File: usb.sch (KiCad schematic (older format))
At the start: 15 parts, among them J3 USB_OTG, Q1 BC817, U2 STMPS2151STR

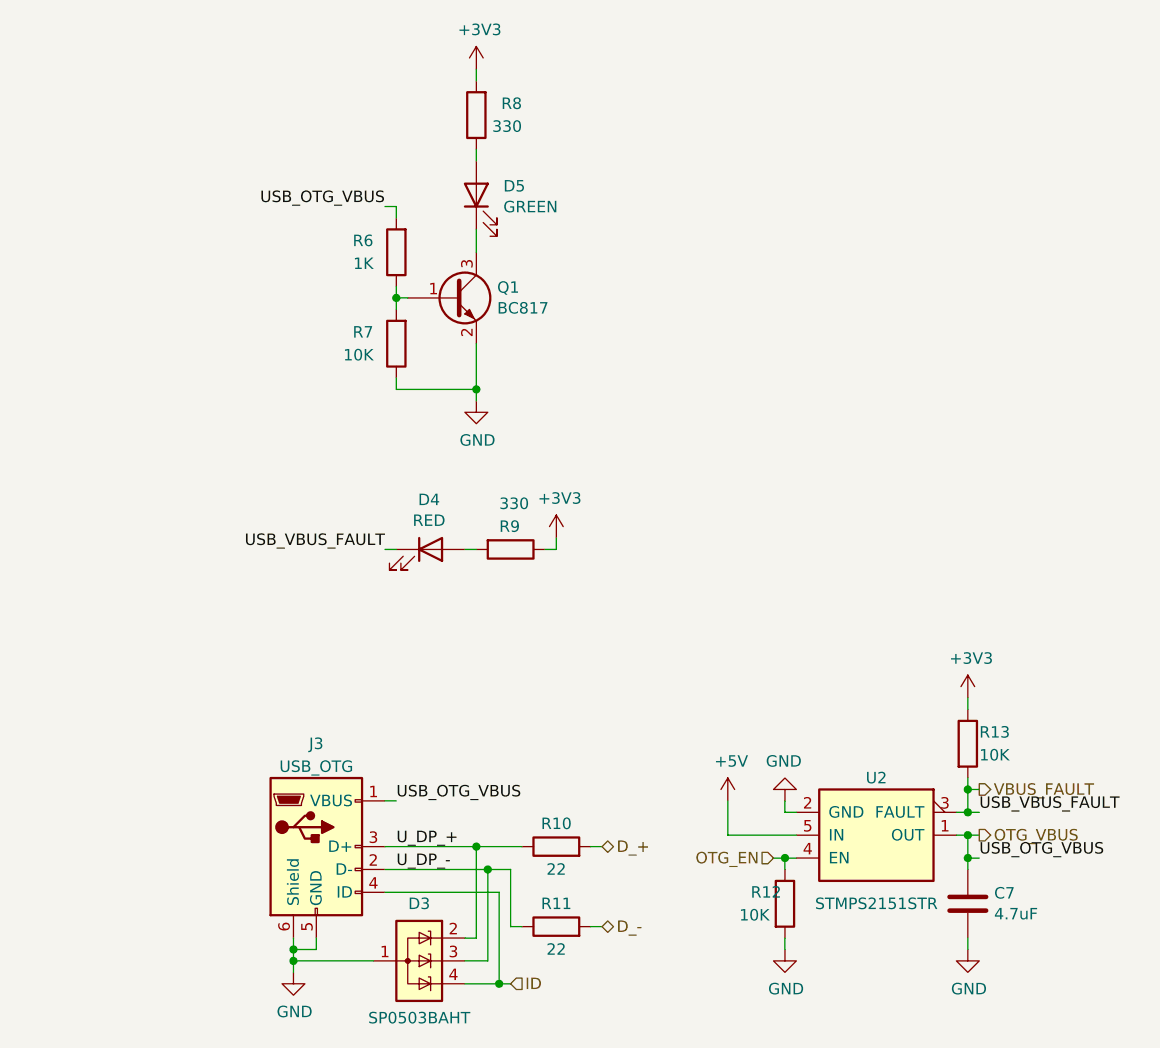
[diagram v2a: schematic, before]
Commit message: dcdc доделан на 5V.
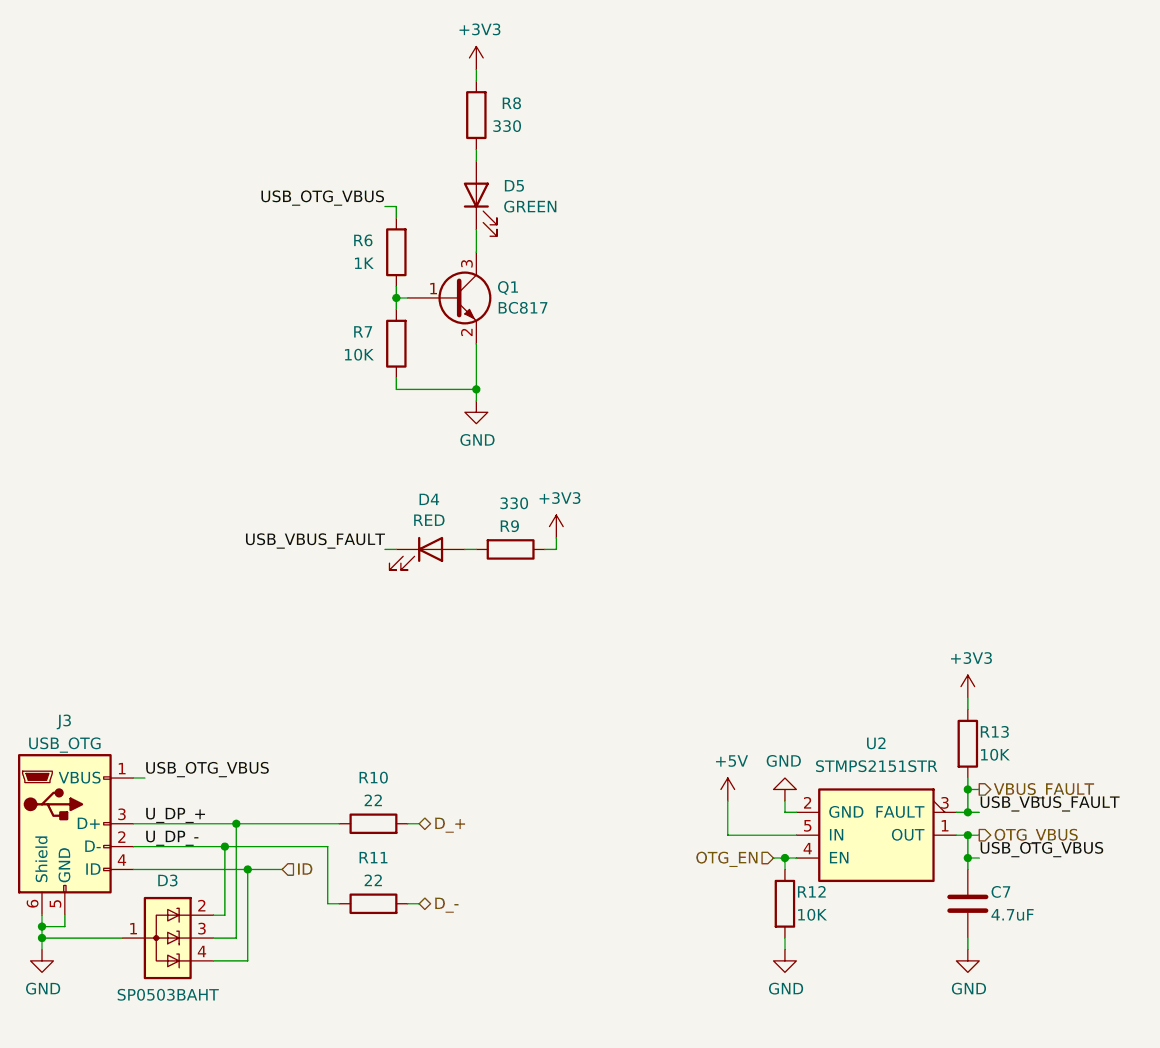
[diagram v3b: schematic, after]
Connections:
- net U_DP_+: now also D3.3 (K); no longer D3.2 (K)
- net U_DP_-: now also D3.2 (K); no longer D3.3 (K)
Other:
- moved on the sheet: D3, J3, R10, R11
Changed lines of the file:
@@
 U 1 1 5EBF34AD
 P 6900 4550
-F 0 "U2" H 7150 4600 50  0000 C CNN
-F 1 "STMPS2151STR" H 7150 4050 50  0000 C CNN
+F 0 "U2" H 7150 4750 50  0000 C CNN
+F 1 "STMPS2151STR" H 7150 4650 50  0000 C CNN
 F 2 "Package_TO_SOT_SMD:SOT-23-5_HandSoldering" H 6950 4600 50  0001 C CNN
 F 3 "" H 6950 4600 50  0001 C CNN
@@
 U 1 1 5EBF34C5
 P 6750 5050
-F 0 "R12" H 6600 5100 50  0000 L CNN
-F 1 "10K" H 6550 5000 50  0000 L CNN
+F 0 "R12" H 6800 5100 50  0000 L CNN
+F 1 "10K" H 6800 5000 50  0000 L CNN
 F 2 "Resistor_SMD:R_0603_1608Metric_Pad1.05x0.95mm_HandSolder" V 6680 5050 50  0001 C CNN
 F 3 "~" H 6750 5050 50  0001 C CNN
@@
 U 1 1 5EBF34D7
 P 7550 5050
-F 0 "C7" H 7665 5096 50  0000 L CNN
-F 1 "4.7uF" H 7665 5005 50  0000 L CNN
+F 0 "C7" H 7650 5100 50  0000 L CNN
+F 1 "4.7uF" H 7650 5000 50  0000 L CNN
 F 2 "Capacitor_SMD:C_0603_1608Metric_Pad1.05x0.95mm_HandSolder" H 7588 4900 50  0001 C CNN
 F 3 "~" H 7550 5050 50  0001 C CNN
@@
 L Connector:USB_OTG J3
 U 1 1 5EBF354C
-P 4700 4800
-F 0 "J3" H 4700 5250 50  0000 C CNN
-F 1 "USB_OTG" H 4700 5150 50  0000 C CNN
-F 2 "Connector_USB:USB_Mini-B_Wuerth_65100516121_Horizontal" H 4850 4750 50  0001 C CNN
-F 3 " ~" H 4850 4750 50  0001 C CNN
-	1    4700 4800
-	1    0    0    -1
-$EndComp
-Wire Wire Line
-	5000 4800 5400 4800
-Wire Wire Line
-	5400 5200 5400 4800
-Connection ~ 5400 4800
-Wire Wire Line
-	5400 4800 5600 4800
-Connection ~ 4600 5300
-Wire Wire Line
-	4600 5350 4600 5300
-Wire Wire Line
-	4600 5300 4950 5300
-Wire Wire Line
-	5450 4900 5550 4900
-Connection ~ 5450 4900
-Wire Wire Line
-	5450 5300 5450 4900
-Connection ~ 5500 5400
-Wire Wire Line
-	5350 5400 5500 5400
-Wire Wire Line
-	5000 5000 5500 5000
-Wire Wire Line
-	5500 5400 5550 5400
-Wire Wire Line
-	5500 5000 5500 5400
-Wire Wire Line
-	5900 5150 5950 5150
-Wire Wire Line
-	5900 4800 5950 4800
-Wire Wire Line
-	5550 5150 5600 5150
-Wire Wire Line
-	5550 4900 5550 5150
-Wire Wire Line
-	5000 4900 5450 4900
+P 3600 4700
+F 0 "J3" H 3600 5150 50  0000 C CNN
+F 1 "USB_OTG" H 3600 5050 50  0000 C CNN
+F 2 "Connector_USB:USB_Mini-B_Wuerth_65100516121_Horizontal" H 3750 4650 50  0001 C CNN
+F 3 " ~" H 3750 4650 50  0001 C CNN
+	1    3600 4700
+	1    0    0    -1
+$EndComp
+Connection ~ 3500 5200
+Wire Wire Line
+	3500 5250 3500 5200
+Wire Wire Line
+	3500 5200 3850 5200
+Wire Wire Line
+	5100 5050 5150 5050
+Wire Wire Line
+	5100 4700 5150 4700
+Wire Wire Line
+	4750 5050 4800 5050
+Wire Wire Line
+	4750 4800 4750 5050
 $Comp
 L Device:R R10
 U 1 1 5EBF356B
-P 5750 4800
-F 0 "R10" V 5850 4800 50  0000 C CNN
-F 1 "22" V 5650 4800 50  0000 C CNN
-F 2 "Resistor_SMD:R_0603_1608Metric_Pad1.05x0.95mm_HandSolder" V 5680 4800 50  0001 C CNN
-F 3 "~" H 5750 4800 50  0001 C CNN
-	1    5750 4800
+P 4950 4700
+F 0 "R10" V 5150 4700 50  0000 C CNN
+F 1 "22" V 5050 4700 50  0000 C CNN
+F 2 "Resistor_SMD:R_0603_1608Metric_Pad1.05x0.95mm_HandSolder" V 4880 4700 50  0001 C CNN
+F 3 "~" H 4950 4700 50  0001 C CNN
+	1    4950 4700
 	0    -1   -1   0
 $EndComp
-Connection ~ 4600 5250
-Wire Wire Line
-	4600 5300 4600 5250
+Connection ~ 3500 5150
+Wire Wire Line
+	3500 5200 3500 5150
 $Comp
 L power:GND #PWR012
 U 1 1 5EBF3573
-P 4600 5350
-F 0 "#PWR012" H 4600 5100 50  0001 C CNN
-F 1 "GND" H 4605 5177 50  0000 C CNN
-F 2 "" H 4600 5350 50  0001 C CNN
-F 3 "" H 4600 5350 50  0001 C CNN
-	1    4600 5350
-	1    0    0    -1
-$EndComp
-Wire Wire Line
-	4700 5250 4700 5200
-Wire Wire Line
-	4600 5250 4700 5250
-Wire Wire Line
-	4600 5200 4600 5250
+P 3500 5250
+F 0 "#PWR012" H 3500 5000 50  0001 C CNN
+F 1 "GND" H 3505 5077 50  0000 C CNN
+F 2 "" H 3500 5250 50  0001 C CNN
+F 3 "" H 3500 5250 50  0001 C CNN
+	1    3500 5250
+	1    0    0    -1
+$EndComp
+Wire Wire Line
+	3600 5150 3600 5100
+Wire Wire Line
+	3500 5150 3600 5150
+Wire Wire Line
+	3500 5100 3500 5150
 $Comp
 L Power_Protection:SP0503BAHT D3
 U 1 1 5EBF357C
-P 5150 5300
-F 0 "D3" V 4900 5300 50  0000 C CNN
-F 1 "SP0503BAHT" V 5400 5300 50  0000 C CNN
-F 2 "Package_TO_SOT_SMD:SOT-143_Handsoldering" H 5375 5250 50  0001 L CNN
-F 3 "http://www.littelfuse.com/~/media/files/littelfuse/technical%20resources/documents/data%20sheets/sp05xxba.pdf" H 5275 5425 50  0001 C CNN
-	1    5150 5300
+P 4050 5200
+F 0 "D3" V 3800 5200 50  0000 C CNN
+F 1 "SP0503BAHT" V 4300 5200 50  0000 C CNN
+F 2 "Package_TO_SOT_SMD:SOT-143_Handsoldering" H 4275 5150 50  0001 L CNN
+F 3 "http://www.littelfuse.com/~/media/files/littelfuse/technical%20resources/documents/data%20sheets/sp05xxba.pdf" H 4175 5325 50  0001 C CNN
+	1    4050 5200
 	0    1    1    0
 $EndComp
@@
 L Device:R R11
 U 1 1 5EBF3583
-P 5750 5150
-F 0 "R11" V 5850 5150 50  0000 C CNN
-F 1 "22" V 5650 5150 50  0000 C CNN
-F 2 "Resistor_SMD:R_0603_1608Metric_Pad1.05x0.95mm_HandSolder" V 5680 5150 50  0001 C CNN
-F 3 "~" H 5750 5150 50  0001 C CNN
-	1    5750 5150
+P 4950 5050
+F 0 "R11" V 5150 5050 50  0000 C CNN
+F 1 "22" V 5050 5050 50  0000 C CNN
+F 2 "Resistor_SMD:R_0603_1608Metric_Pad1.05x0.95mm_HandSolder" V 4880 5050 50  0001 C CNN
+F 3 "~" H 4950 5050 50  0001 C CNN
+	1    4950 5050
 	0    -1   -1   0
 $EndComp
 Wire Wire Line
-	5000 4600 5050 4600
+	3900 4500 3950 4500
 Text HLabel 7600 4550 2    50   Output ~ 0
 VBUS_FAULT
@@
 Text Label 7600 4850 0    50   ~ 0
 USB_OTG_VBUS
-Text Label 5050 4600 0    50   ~ 0
+Text Label 3950 4500 0    50   ~ 0
 USB_OTG_VBUS
-Text HLabel 5950 4800 2    50   BiDi ~ 0
+Text HLabel 5150 4700 2    50   BiDi ~ 0
 D_+
-Text HLabel 5950 5150 2    50   BiDi ~ 0
+Text HLabel 5150 5050 2    50   BiDi ~ 0
 D_-
-Text HLabel 5550 5400 2    50   Input ~ 0
+Text HLabel 4550 4900 2    50   Input ~ 0
 ID
 Text Label 7600 4650 0    50   ~ 0
@@
 	5400 2800 5400 2850
 Connection ~ 5400 2800
-Text Label 5050 4800 0    50   ~ 0
+Text Label 3950 4700 0    50   ~ 0
 U_DP_+
-Text Label 5050 4900 0    50   ~ 0
+Text Label 3950 4800 0    50   ~ 0
 U_DP_-
 Wire Wire Line
-	5350 5300 5450 5300
-Wire Wire Line
-	5350 5200 5400 5200
+	4250 5100 4300 5100
+Wire Wire Line
+	4250 5300 4400 5300
+Wire Wire Line
+	4400 4900 4550 4900
+Wire Wire Line
+	3900 4900 4400 4900
+Connection ~ 4400 4900
+Wire Wire Line
+	3900 4700 4350 4700
+Wire Wire Line
+	3900 4800 4300 4800
+Wire Wire Line
+	4300 5100 4300 4800
+Connection ~ 4300 4800
+Wire Wire Line
+	4300 4800 4750 4800
+Wire Wire Line
+	4400 4900 4400 5300
+Wire Wire Line
+	4250 5200 4350 5200
+Wire Wire Line
+	4350 5200 4350 4700
+Connection ~ 4350 4700
+Wire Wire Line
+	4350 4700 4800 4700
 $EndSCHEMATC

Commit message: Расставил проверенные блоки в столбец.
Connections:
- net OTG_VBUS renamed VDD_USB
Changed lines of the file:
@@
 $Descr A4 11693 8268
 encoding utf-8
-Sheet 9 12
+Sheet 8 12
 Title ""
 Date ""
@@
 $EndComp
 Wire Wire Line
-	7550 4900 7550 4850
-Wire Wire Line
 	7550 4750 7600 4750
 Connection ~ 7550 4750
@@
 U 1 1 5EBF34F9
 P 5200 3500
-F 0 "D4" H 5193 3717 50  0000 C CNN
-F 1 "RED" H 5193 3626 50  0000 C CNN
+F 0 "D4" H 5200 3700 50  0000 C CNN
+F 1 "RED" H 5200 3600 50  0000 C CNN
 F 2 "LED_SMD:LED_0603_1608Metric_Pad1.05x0.95mm_HandSolder" H 5200 3500 50  0001 C CNN
 F 3 "~" H 5200 3500 50  0001 C CNN
@@
 U 1 1 5EBF34FF
 P 5550 3500
-F 0 "R9" V 5450 3450 50  0000 L CNN
-F 1 "330" V 5350 3450 50  0000 L CNN
+F 0 "R9" V 5350 3450 50  0000 L CNN
+F 1 "330" V 5450 3425 50  0000 L CNN
 F 2 "Resistor_SMD:R_0603_1608Metric_Pad1.05x0.95mm_HandSolder" V 5480 3500 50  0001 C CNN
 F 3 "~" H 5550 3500 50  0001 C CNN
@@
 P 5750 3450
 F 0 "#PWR015" H 5750 3300 50  0001 C CNN
-F 1 "+3V3" H 5765 3623 50  0000 C CNN
+F 1 "+3V3" H 5750 3650 50  0000 C CNN
 F 2 "" H 5750 3450 50  0001 C CNN
 F 3 "" H 5750 3450 50  0001 C CNN
@@
 U 1 1 5EBF3510
 P 5050 2200
-F 0 "R6" H 5150 2150 50  0000 L CNN
-F 1 "1K" H 5150 2250 50  0000 L CNN
+F 0 "R6" H 4900 2150 50  0000 L CNN
+F 1 "1K" H 4900 2250 50  0000 L CNN
 F 2 "Resistor_SMD:R_0603_1608Metric_Pad1.05x0.95mm_HandSolder" V 4980 2200 50  0001 C CNN
 F 3 "~" H 5050 2200 50  0001 C CNN
@@
 U 1 1 5EBF3516
 P 5050 2600
-F 0 "R7" H 5150 2550 50  0000 L CNN
-F 1 "10K" H 5150 2650 50  0000 L CNN
+F 0 "R7" H 4900 2550 50  0000 L CNN
+F 1 "10K" H 4850 2650 50  0000 L CNN
 F 2 "Resistor_SMD:R_0603_1608Metric_Pad1.05x0.95mm_HandSolder" V 4980 2600 50  0001 C CNN
 F 3 "~" H 5050 2600 50  0001 C CNN
@@
 U 1 1 5EBF351C
 P 5400 1600
-F 0 "R8" H 5200 1550 50  0000 L CNN
+F 0 "R8" H 5250 1550 50  0000 L CNN
 F 1 "330" H 5200 1650 50  0000 L CNN
 F 2 "Resistor_SMD:R_0603_1608Metric_Pad1.05x0.95mm_HandSolder" V 5330 1600 50  0001 C CNN
@@
 U 1 1 5EBF3533
 P 5400 1950
-F 0 "D5" V 5439 1832 50  0000 R CNN
-F 1 "GREEN" V 5348 1832 50  0000 R CNN
+F 0 "D5" V 5450 1900 50  0000 R CNN
+F 1 "GREEN" V 5350 1900 50  0000 R CNN
 F 2 "LED_SMD:LED_0603_1608Metric_Pad1.05x0.95mm_HandSolder" H 5400 1950 50  0001 C CNN
 F 3 "~" H 5400 1950 50  0001 C CNN
@@
 	0    -1   -1   0
 $EndComp
-Wire Wire Line
-	3900 4500 3950 4500
 Text HLabel 7600 4550 2    50   Output ~ 0
 VBUS_FAULT
-Text HLabel 7600 4750 2    50   Output ~ 0
-OTG_VBUS
-Wire Wire Line
-	7550 4850 7600 4850
-Connection ~ 7550 4850
-Wire Wire Line
-	7550 4850 7550 4750
-Text Label 7600 4850 0    50   ~ 0
+Text HLabel 4000 4500 2    50   Output ~ 0
+VDD_USB
+Text Label 7600 4750 0    50   ~ 0
 USB_OTG_VBUS
-Text Label 3950 4500 0    50   ~ 0
+Text Label 4000 4400 0    50   ~ 0
 USB_OTG_VBUS
 Text HLabel 5150 4700 2    50   BiDi ~ 0
@@
 Wire Wire Line
 	4350 4700 4800 4700
+Wire Wire Line
+	7550 4750 7550 4900
+Wire Wire Line
+	3900 4500 3950 4500
+Wire Wire Line
+	3950 4500 3950 4400
+Wire Wire Line
+	3950 4400 4000 4400
+Connection ~ 3950 4500
+Wire Wire Line
+	3950 4500 4000 4500
 $EndSCHEMATC
